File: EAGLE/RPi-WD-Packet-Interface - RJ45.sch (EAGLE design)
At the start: 29 parts, among them IC1 TLC555, Q1 PTT, Q2 PTT-LED, Q3 DCD-LED

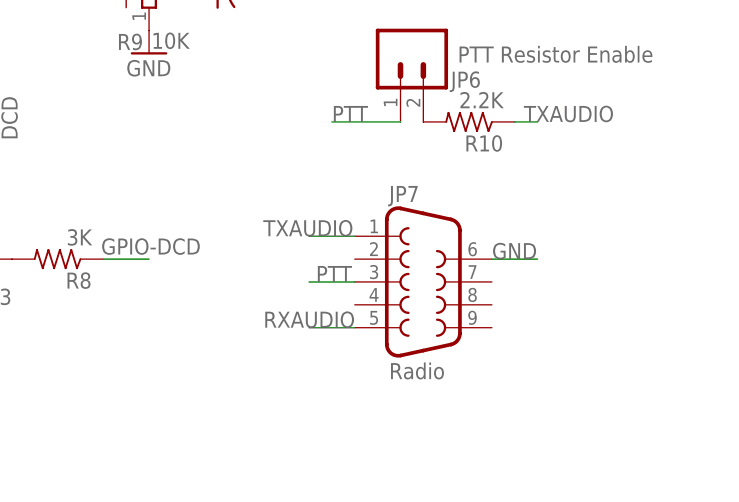
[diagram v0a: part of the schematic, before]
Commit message: Replace DB-9 files with RJ-45 version 1.0
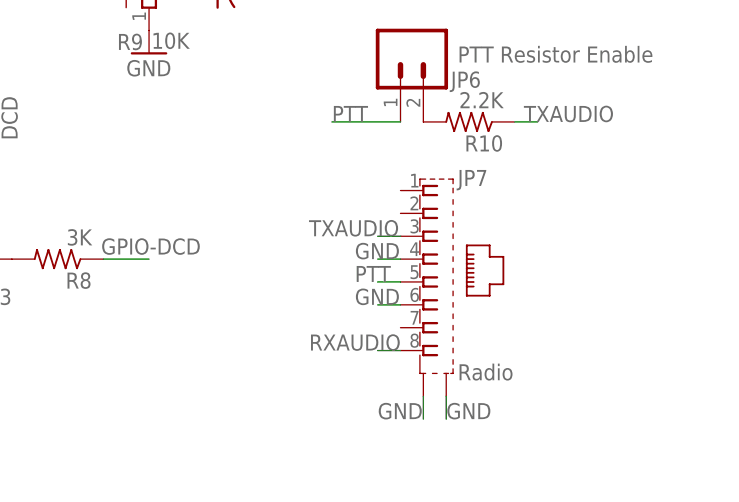
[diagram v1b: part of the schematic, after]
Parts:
- JP7: device SparkFun-Connectors:DB9FEMALE -> con-molex:0446200002
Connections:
- net GND: now also JP7.4, JP7.S1, JP7.S2
- net PTT: now also JP7.5; no longer JP7.3
- net RXAUDIO: now also JP7.8; no longer JP7.5
- net TXAUDIO: now also JP7.3; no longer JP7.1
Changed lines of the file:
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@@
 <?xml version="1.0" encoding="utf-8"?>
 <!DOCTYPE eagle SYSTEM "eagle.dtd">
-<eagle version="7.3.0">
+<eagle version="9.1.0">
 <drawing>
 <settings>
 <setting alwaysvectorfont="no"/>
+<setting keepoldvectorfont="yes"/>
 <setting verticaltext="up"/>
 </settings>
@@
 <part name="Q3" library="SparkFun-DiscreteSemi" deviceset="TRANSISTOR_NPN" device="TO-92-AMMO" value="DCD-LED"/>
 <part name="GND9" library="SparkFun-Aesthetics" deviceset="GND" device=""/>
-<part name="JP7" library="SparkFun-Connectors" deviceset="DB9" device="FEMALE" value="Radio"/>
+<part name="JP7" library="con-molex" library_urn="urn:adsk.eagle:library:165" deviceset="0446200002" device="" value="Radio"/>
 <part name="GND2" library="SparkFun-Aesthetics" deviceset="GND" device=""/>
 <part name="R1" library="rcl" deviceset="R-US_" device="0207/7" value="10K"/>
@@
 </instance>
 <instance part="GND9" gate="1" x="109.22" y="27.94"/>
-<instance part="JP7" gate="G$1" x="160.02" y="33.02"/>
+<instance part="JP7" gate="P" x="160.02" y="33.02"/>
 <instance part="GND2" gate="1" x="5.08" y="45.72"/>
 <instance part="R1" gate="G$1" x="38.1" y="55.88" rot="R270"/>
@@
 </segment>
 <segment>
-<pinref part="JP7" gate="G$1" pin="3"/>
-<wire x1="152.4" y1="33.02" x2="147.32" y2="33.02" width="0.1524" layer="91"/>
-<label x="148.082" y="33.02" size="1.778" layer="95"/>
+<pinref part="JP7" gate="P" pin="5"/>
+<wire x1="157.48" y1="33.02" x2="154.94" y2="33.02" width="0.1524" layer="91"/>
+<label x="152.4" y="33.02" size="1.778" layer="95"/>
 </segment>
 </net>
@@
 </segment>
 <segment>
-<pinref part="JP7" gate="G$1" pin="1"/>
-<wire x1="152.4" y1="38.1" x2="147.32" y2="38.1" width="0.1524" layer="91"/>
-<label x="142.24" y="38.1" size="1.778" layer="95"/>
+<pinref part="JP7" gate="P" pin="3"/>
+<wire x1="157.48" y1="38.1" x2="154.94" y2="38.1" width="0.1524" layer="91"/>
+<label x="147.32" y="38.1" size="1.778" layer="95"/>
 </segment>
 </net>
 <net name="RXAUDIO" class="0">
-<segment>
-<pinref part="JP7" gate="G$1" pin="5"/>
-<wire x1="152.4" y1="27.94" x2="147.32" y2="27.94" width="0.1524" layer="91"/>
-<label x="142.24" y="27.94" size="1.778" layer="95"/>
-</segment>
 <segment>
 <pinref part="JP1" gate="G$1" pin="2"/>
 <wire x1="-2.54" y1="20.32" x2="0" y2="20.32" width="0.1524" layer="91"/>
 <label x="-2.54" y="20.32" size="1.778" layer="95"/>
+</segment>
+<segment>
+<pinref part="JP7" gate="P" pin="8"/>
+<wire x1="157.48" y1="25.4" x2="154.94" y2="25.4" width="0.1524" layer="91"/>
+<label x="147.32" y="25.4" size="1.778" layer="95"/>
 </segment>
 </net>
@@
 </segment>
 <segment>
-<pinref part="JP7" gate="G$1" pin="6"/>
-<wire x1="167.64" y1="35.56" x2="172.72" y2="35.56" width="0.1524" layer="91"/>
-<label x="167.64" y="35.56" size="1.778" layer="95"/>
+<pinref part="JP7" gate="P" pin="4"/>
+<wire x1="157.48" y1="35.56" x2="154.94" y2="35.56" width="0.1524" layer="91"/>
+<label x="152.4" y="35.56" size="1.778" layer="95"/>
+</segment>
+<segment>
+<pinref part="JP7" gate="P" pin="6"/>
+<wire x1="157.48" y1="30.48" x2="154.94" y2="30.48" width="0.1524" layer="91"/>
+<label x="152.4" y="30.48" size="1.778" layer="95"/>
+</segment>
+<segment>
+<pinref part="JP7" gate="P" pin="S1"/>
+<wire x1="160.02" y1="20.32" x2="160.02" y2="17.78" width="0.1524" layer="91"/>
+<label x="154.94" y="17.78" size="1.778" layer="95"/>
+</segment>
+<segment>
+<pinref part="JP7" gate="P" pin="S2"/>
+<wire x1="162.56" y1="20.32" x2="162.56" y2="17.78" width="0.1524" layer="91"/>
+<label x="162.56" y="17.78" size="1.778" layer="95"/>
 </segment>
 </net>
@@
 </schematic>
 </drawing>
+<compatibility>
+<note version="8.2" severity="warning">
+Since Version 8.2, EAGLE supports online libraries. The ids
+of those online libraries will not be understood (or retained)
+with this version.
+</note>
+</compatibility>
 </eagle>
